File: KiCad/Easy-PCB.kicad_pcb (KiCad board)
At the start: 2 copper layers, 203.2 x 96.5 mm, 97 parts, among them J1 703W-00/53, J3 HLW20R-2C7LF, K1 G5LE-1A-E_DC12, P1 1x02, P12 M20-9980346, P2 1x06, P24 M20-9980346, P3 1x04, P4 1x03 Terminal Block, P5 1x02, Q1 2N3904, Q10 MJE350, Q11 2N3904, Q12 2N3904, Q13 MJE340, Q14 MJE350, Q15 2N3904, Q16 MJE340, Q17 MJE350, Q18 2N3904, Q19 2N3904, Q2 MJE340, Q3 2N3904, Q4 2N3904, Q5 MJE340, Q6 MJE350, Q7 2N3904, Q8 2N3904, Q9 MJE340, SW1 R1966ABLKBLKFR, T1 VPP24-830, U1 PIC16F883, U2 MCP41050, U3 MCP617, U4 MCP9700A, U5 LM7805

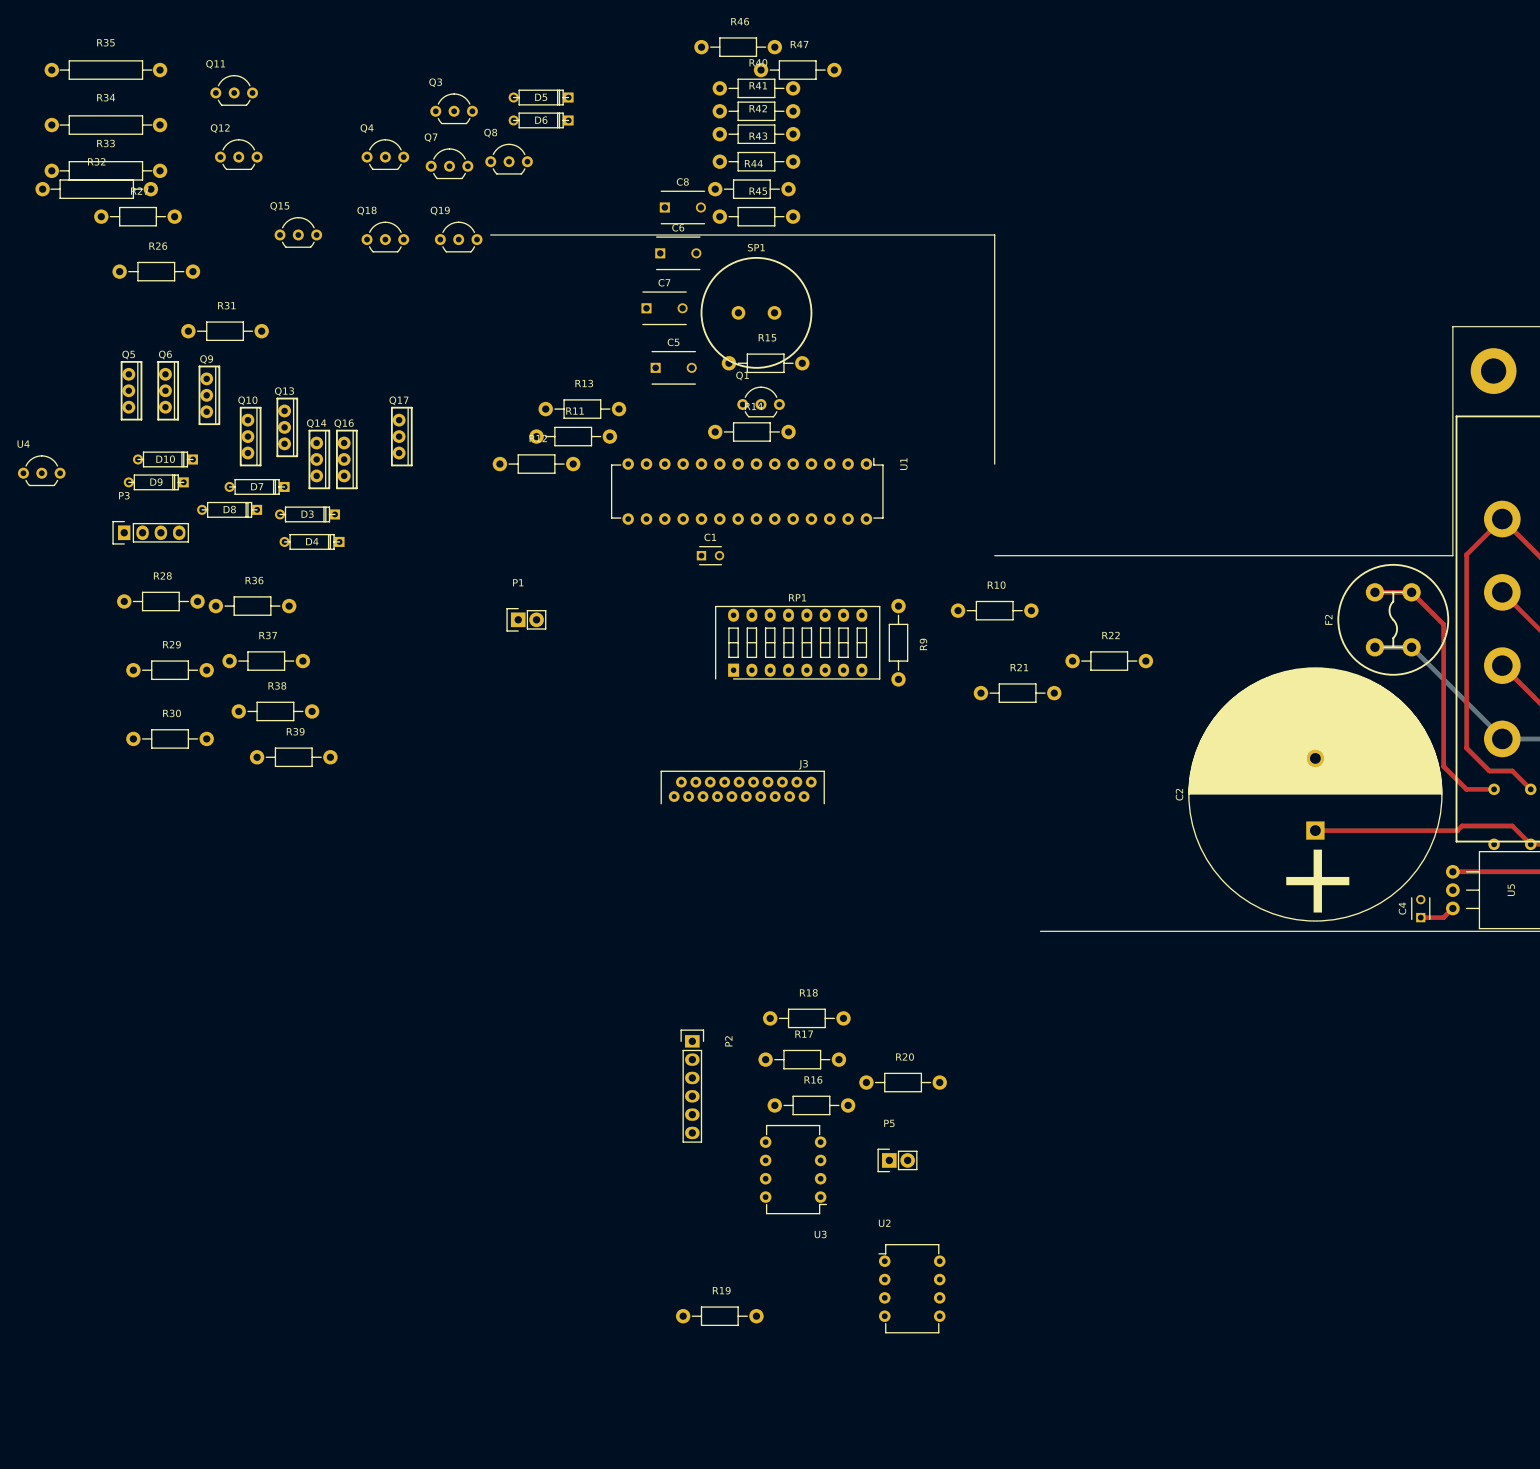
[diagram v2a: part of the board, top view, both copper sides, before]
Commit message: power transistors mostly in place
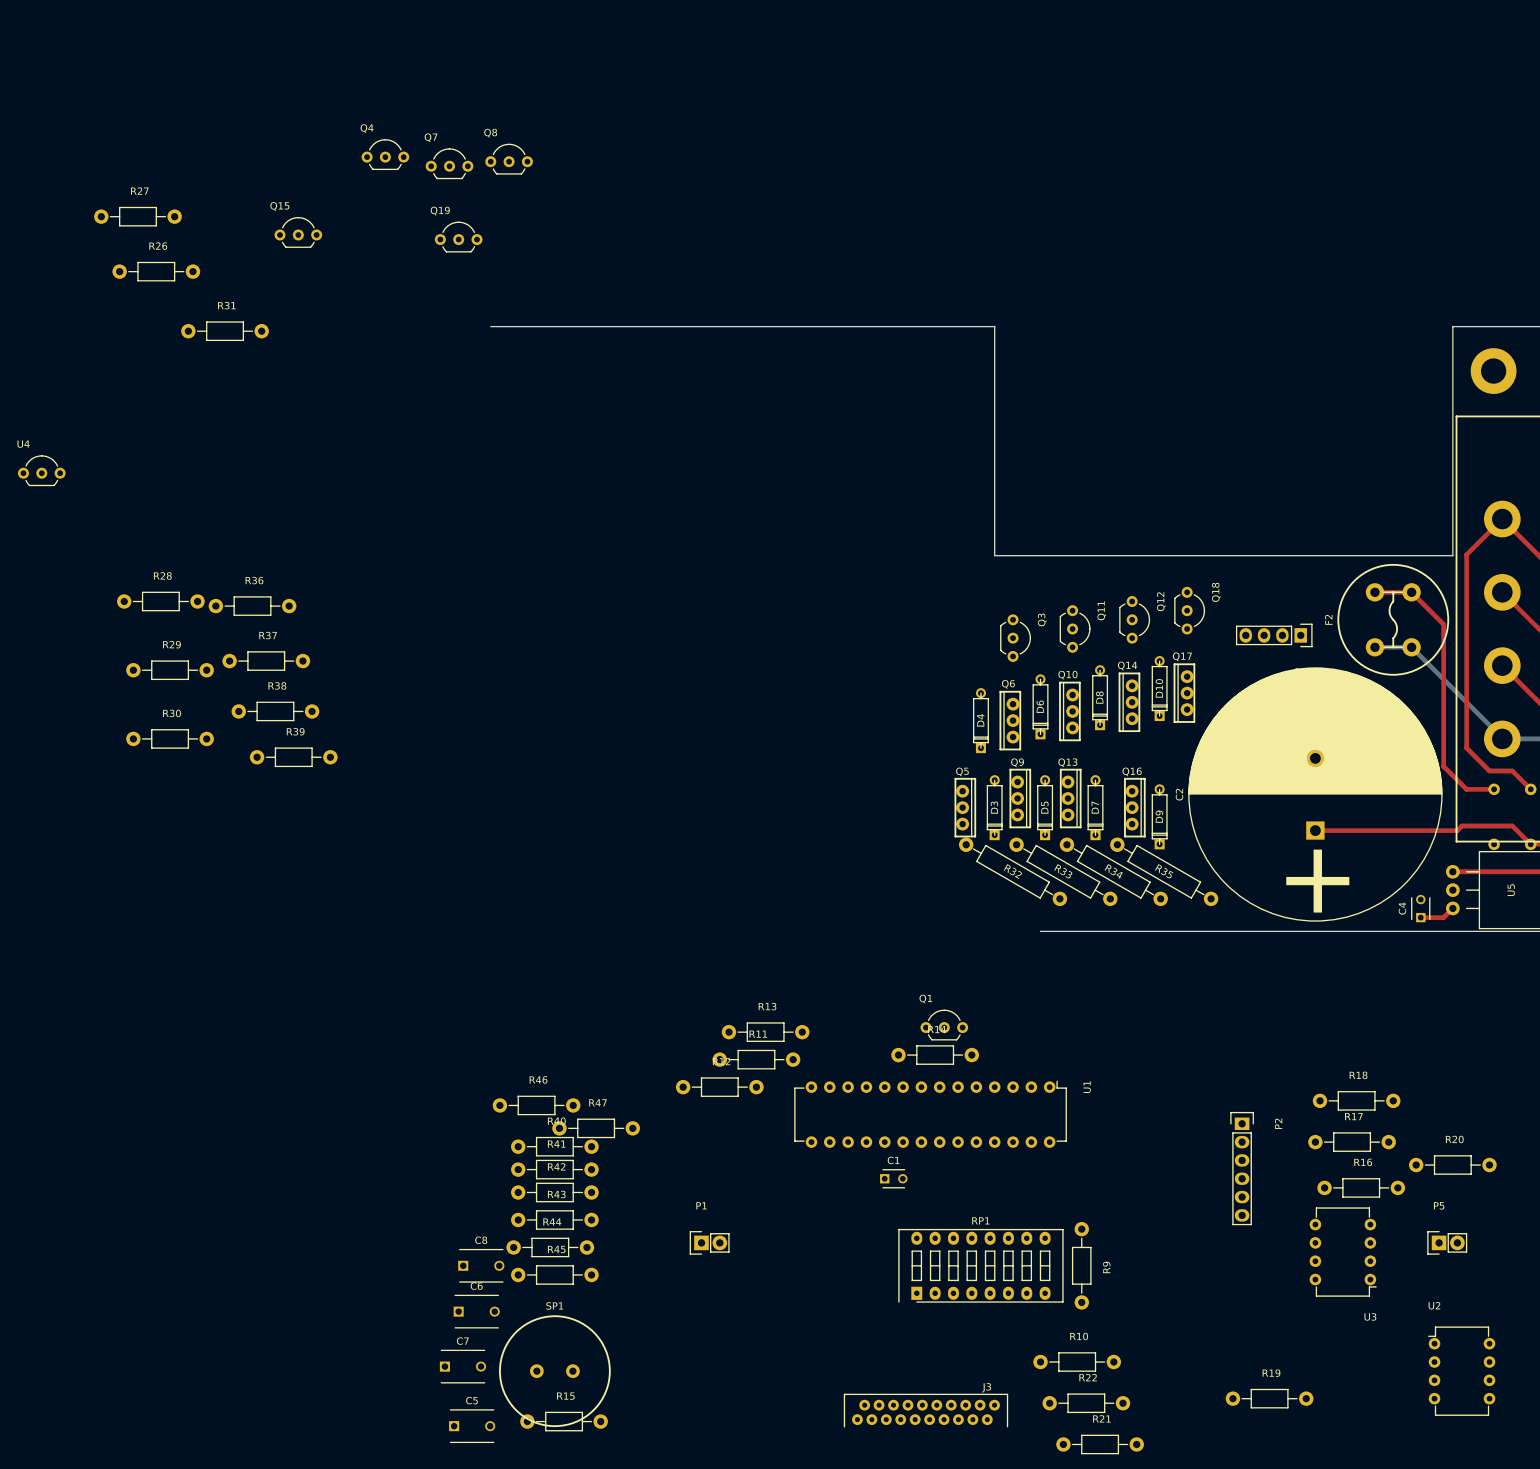
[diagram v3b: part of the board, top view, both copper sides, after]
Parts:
- moved R35 184.0 mm to (118.7, 113.7), turned to 150 degrees
- moved R34 173.9 mm to (111.8, 113.7), turned to 150 degrees
- moved R33 164.5 mm to (104.8, 113.7), turned to 150 degrees
- moved P3 163.7 mm to (137.7, 80.9), turned to 180 degrees
- moved R32 158.4 mm to (97.8, 113.7), turned to 150 degrees
- moved C5 149.3 mm to (20.3, 190.5)
- moved C6 149.3 mm to (21.0, 174.6)
- moved C7 149.3 mm to (19.1, 182.2)
- moved C8 149.3 mm to (21.6, 168.3)
- moved R15 149.3 mm to (35.6, 189.9)
- moved R41 149.3 mm to (34.3, 154.9)
- moved R42 149.3 mm to (34.3, 158.1)
- moved R43 149.3 mm to (34.3, 161.9)
- moved R44 149.3 mm to (33.7, 165.7)
- moved R45 149.3 mm to (34.3, 169.5)
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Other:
- board size 203.2 x 96.5 mm -> 203.2 x 83.8 mm

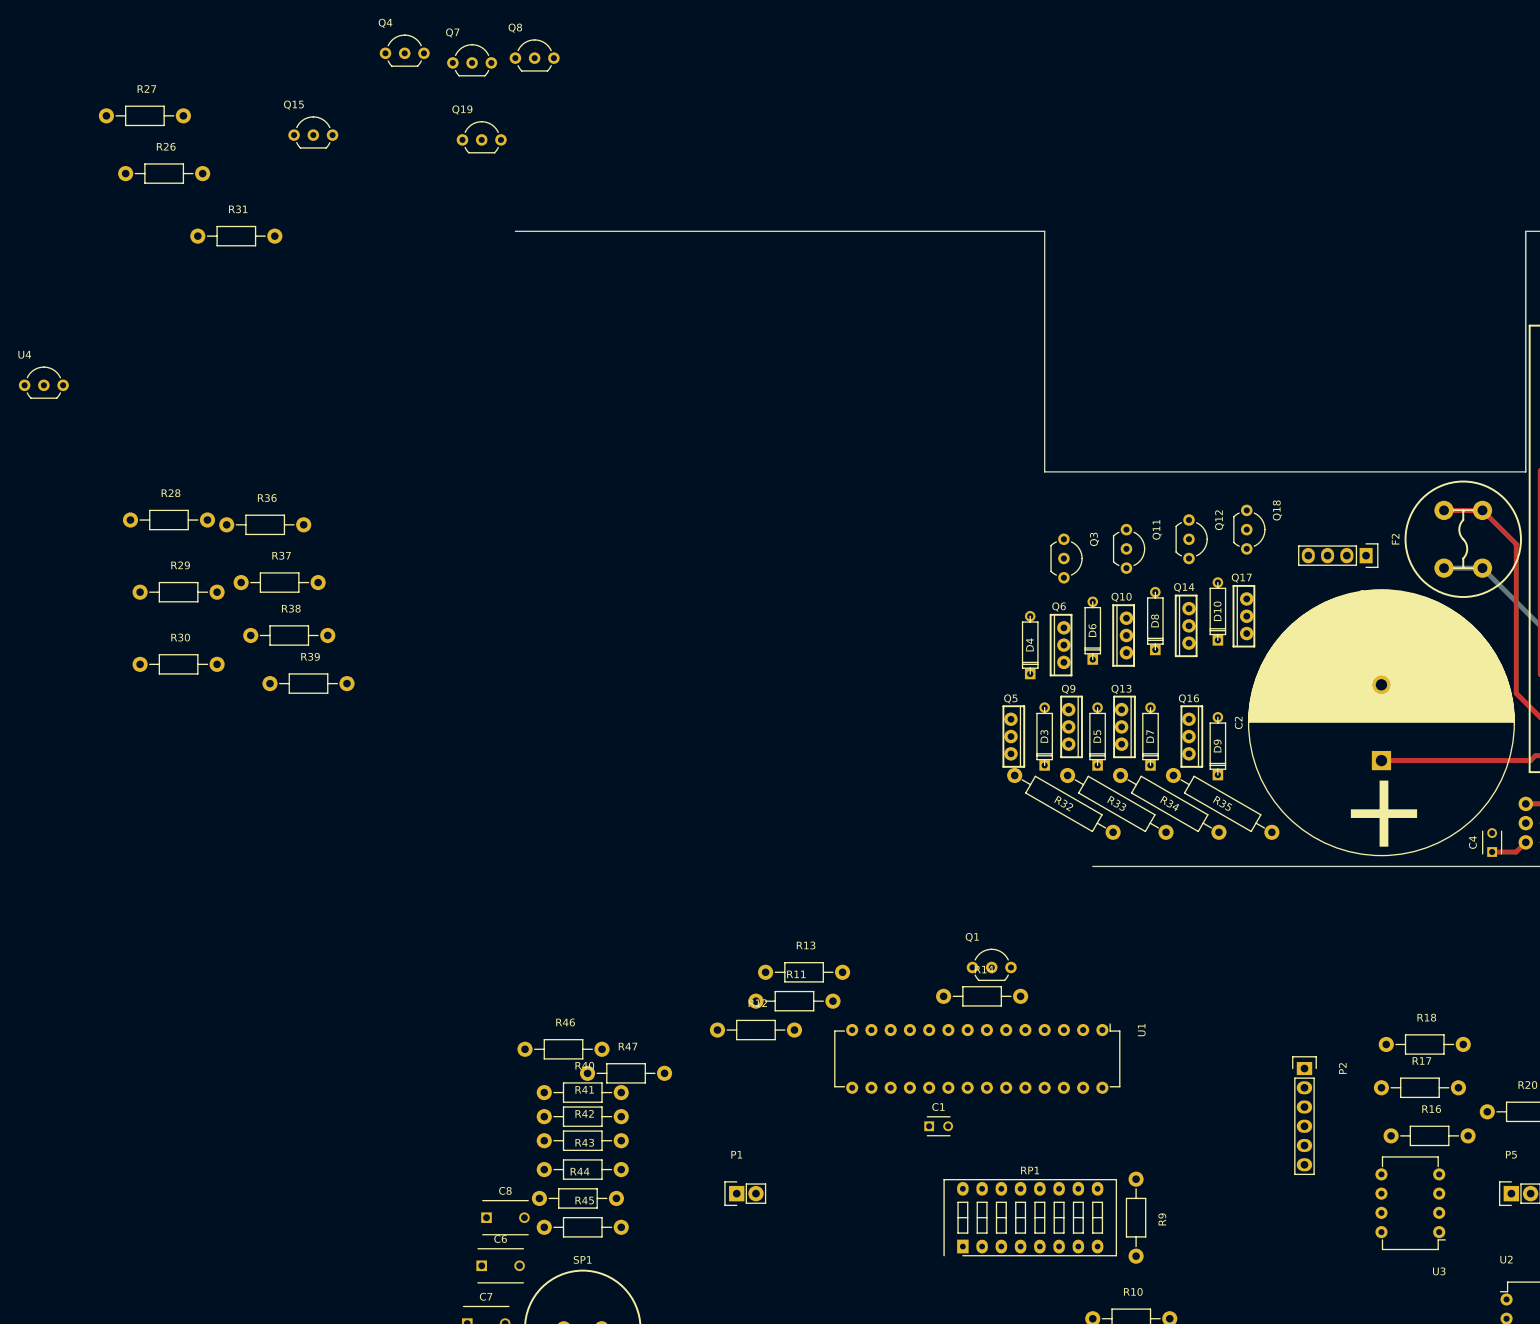
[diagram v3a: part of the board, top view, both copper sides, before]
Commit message: motor circuit routed
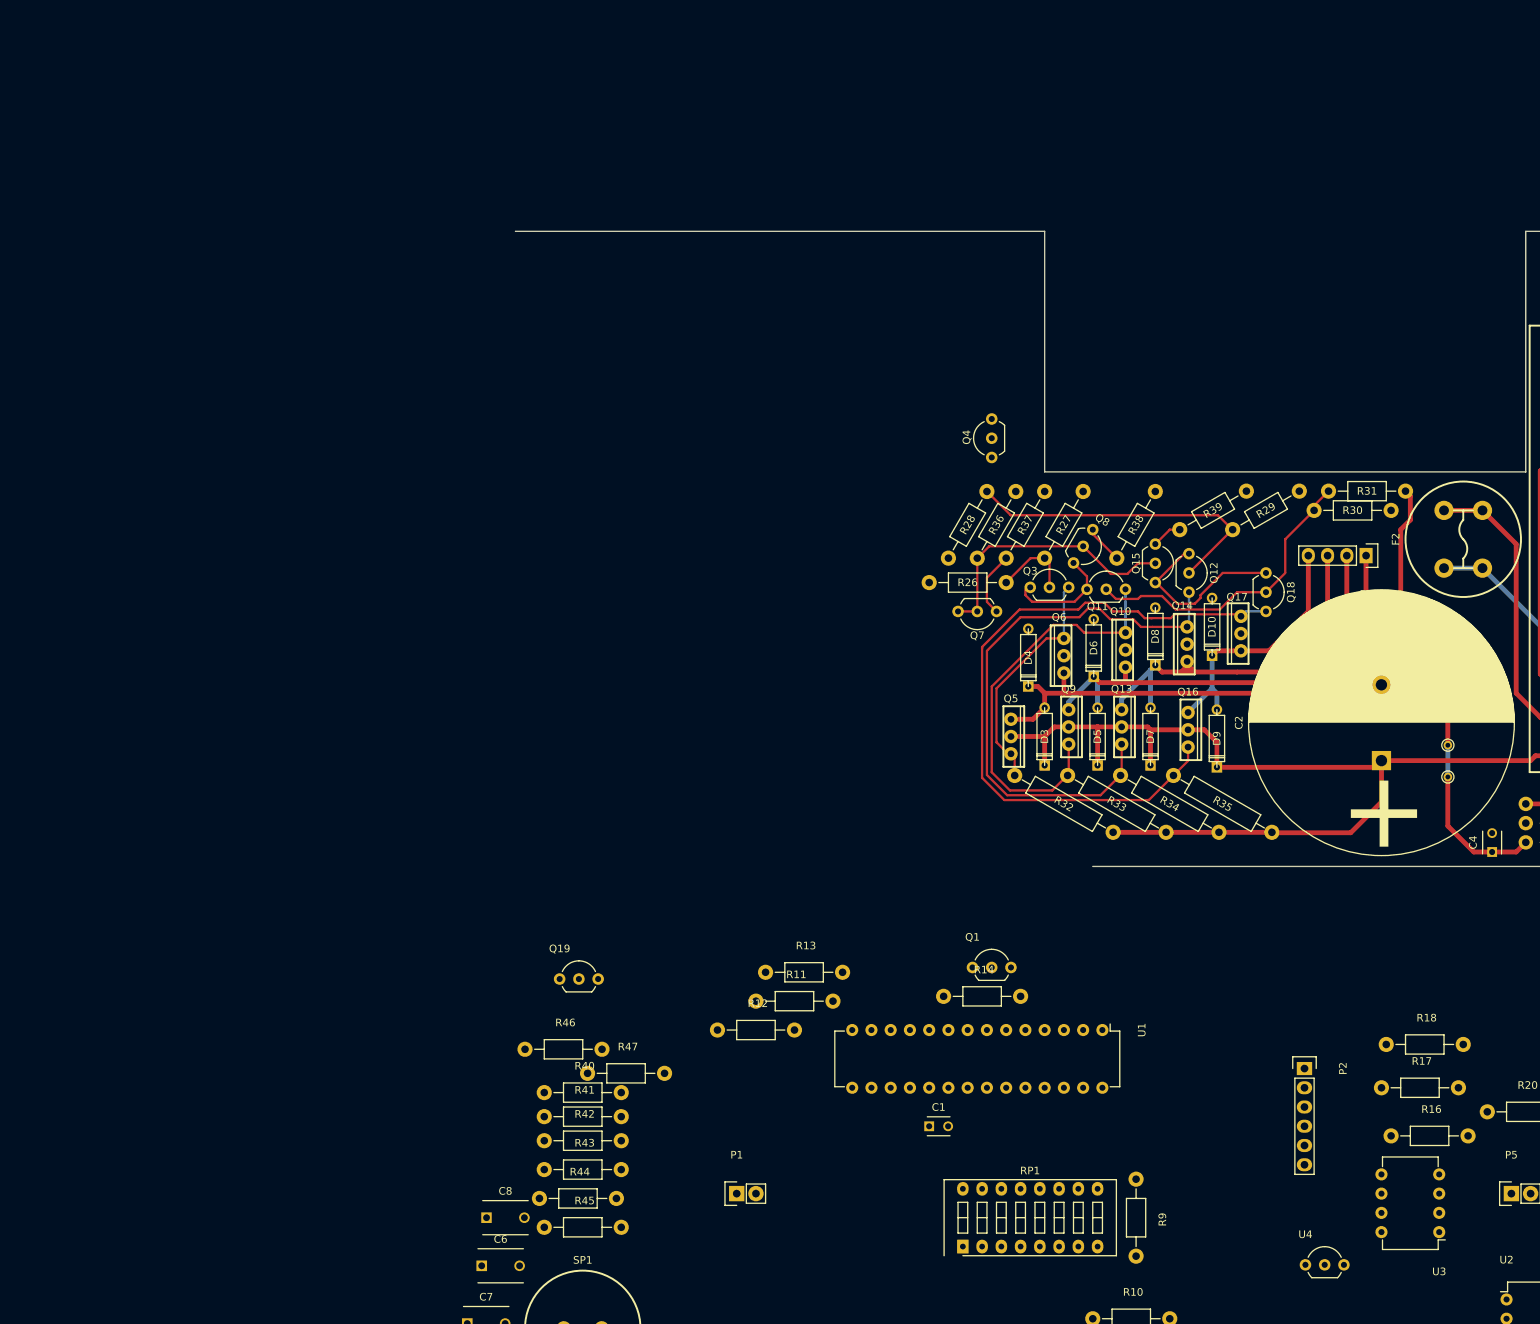
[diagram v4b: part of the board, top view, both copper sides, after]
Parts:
- added P6: via, Connect:PINTST, F.Cu at (148.5, 110.1)
- added P7: via, Connect:PINTST, F.Cu at (148.5, 105.9)
- moved U4 205.1 mm to (129.7, 174.5)
- moved R30 158.5 mm to (137.8, 72.4), turned to 180 degrees
- moved R31 151.7 mm to (135.9, 74.9)
- moved R29 143.9 mm to (124.5, 74.9), turned to 210 degrees
- moved R27 132.8 mm to (97.8, 76.8), turned to 60 degrees
- moved Q15 125.8 mm to (109.9, 79.4), turned to 270 degrees
- moved R39 121.5 mm to (117.5, 74.9), turned to 30 degrees
- moved R26 119.0 mm to (85.1, 84.5), turned to 180 degrees
- moved R38 112.7 mm to (107.3, 76.8), turned to 60 degrees
- moved Q19 111.5 mm to (31.2, 136.8)
- moved R28 105.4 mm to (85.1, 76.8), turned to 240 degrees
- moved Q7 101.9 mm to (88.9, 88.3), turned to 180 degrees
- moved R37 98.7 mm to (92.7, 76.8), turned to 60 degrees
- moved Q8 98.4 mm to (101.6, 77.5), turned to 240 degrees
- moved R36 96.5 mm to (88.9, 76.8), turned to 60 degrees
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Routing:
- net VCC: track 71.7 -> 182.1 mm
- net Net-(Q16-Pad3): track 0.00 -> 90.9 mm
- net Net-(Q12-Pad3): track 0.00 -> 74.8 mm
- net /Motor Driver/wind1a: track 0.18 -> 65.5 mm
- net /Motor Driver/wind1b: track 0.00 -> 56.6 mm
- net VDD: track 4.97 -> 59.8 mm
- net Net-(Q10-Pad3): track 0.00 -> 54.5 mm
- net /Motor Driver/wind2a: track 0.00 -> 52.2 mm
- net Net-(Q12-Pad2): track 0.00 -> 42.6 mm
- net Net-(Q11-Pad2): track 0.00 -> 40.8 mm
- net Net-(Q15-Pad2): track 0.00 -> 35.8 mm
- net /Motor Driver/wind2b: track 0.00 -> 34.4 mm
- net Net-(Q3-Pad3): track 0.00 -> 31.3 mm
- net Net-(Q12-Pad1): track 0.00 -> 23.7 mm
- net Net-(Q11-Pad1): track 0.00 -> 14.2 mm
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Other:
- net class Default: trace_width 0.25 -> 0.3048
